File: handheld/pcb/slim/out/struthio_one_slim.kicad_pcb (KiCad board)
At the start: 2 copper layers, 67.6 x 105.2 mm, 12 parts, among them J1 Header_2x16_Waveshare, J2 S2B-PH-K-S, Q1 AO3401A, Q2 AO3400A, SW1 TS-1187A-B-A-B, SW2 TS-1187A-B-A-B, SW3 TS-1187A-B-A-B, SW4 TS-1187A-B-A-B, SW5 SS-12D06-G030

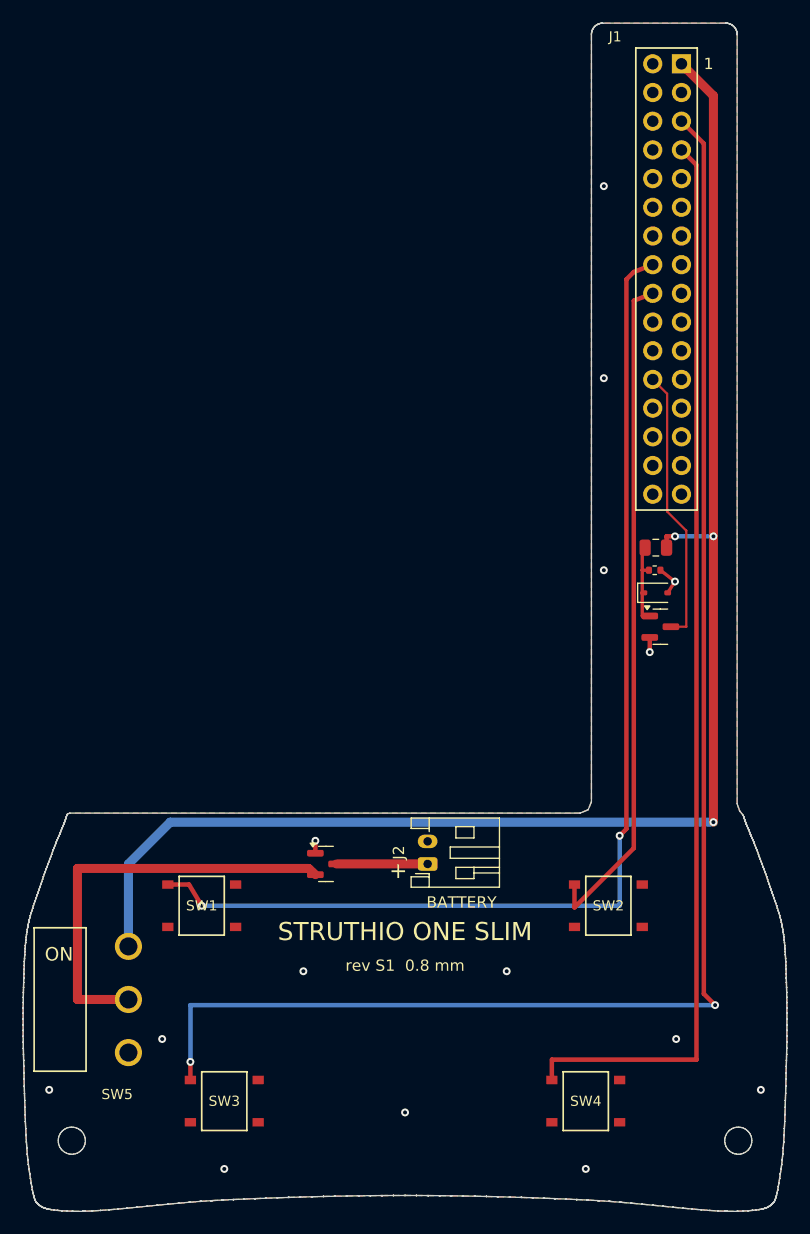
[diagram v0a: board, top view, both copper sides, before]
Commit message: ONE SLIM rev S2 hardware (foolproof) and ONE board rev D
SLIM case: no slide switch; a printed plunger in the left wall presses the Waveshare's
PWR key; one screw size (5 x M2 x 6 countersunk); surface-mount battery socket (no
leads to trim); lead clips; pins stand 3.6 mm out so either socket height works
(3.6 / 2.5 mm into J8), no spacer, no measuring; keyed pin jig (fence + two pegs a
turned-over board cannot sit on) with an 11 mm axle gauge; panel jig. 61 checks pass.
SLIM board rev S2: SW1-4, J2 (C295747), Q1 only, all surface-mount; pin 9 open.
ONE board rev D: header pin 9 tied to GND (the firmware's model strap).
Both boards: DRC no errors, no unconnected pads.

Co-Authored-By: Claude Opus 5.5 <noreply@anthropic.com>
Claude-Session: https://claude.ai/code/session_01BN2x2AjDXTm5ZbuwkUnxX5
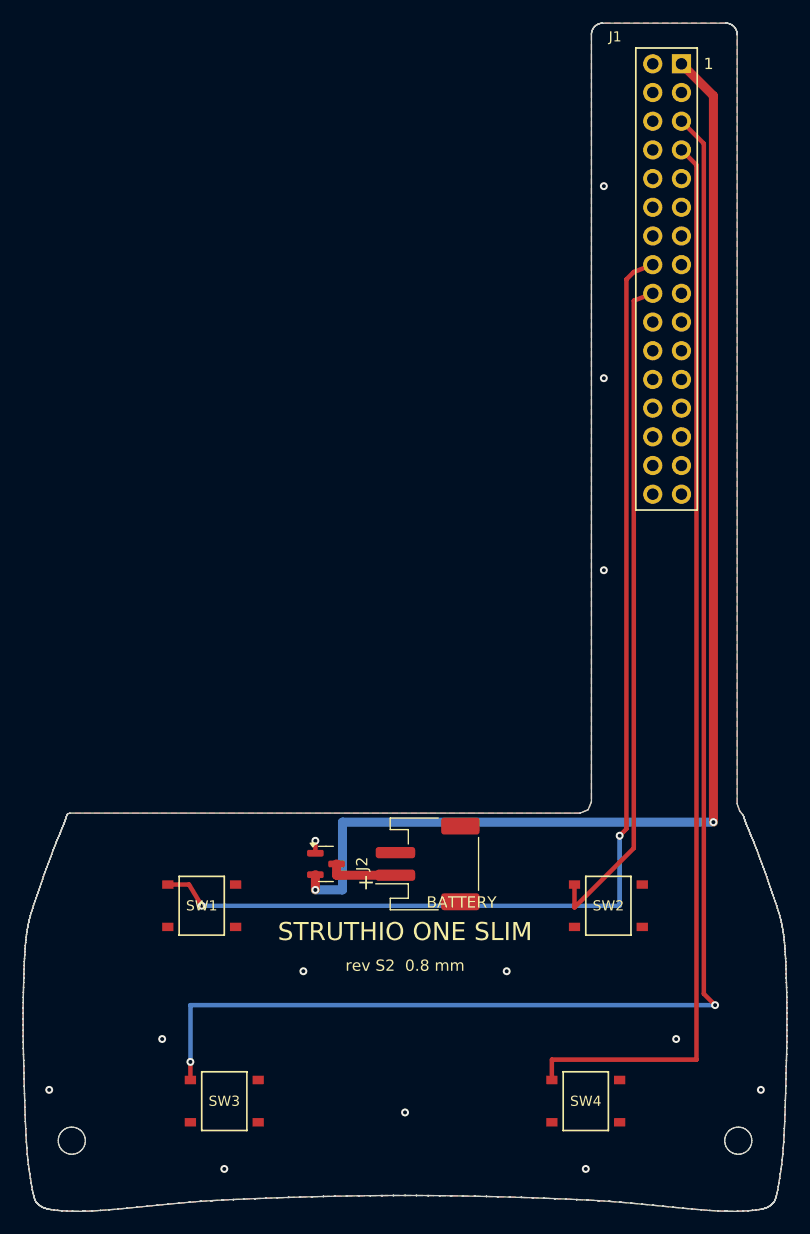
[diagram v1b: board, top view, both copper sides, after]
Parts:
- removed C1: 10uF, C_0805_2012Metric
- removed D1: 1N4148WS, D_SOD-323
- removed Q2: AO3400A, SOT-23
- removed R1: 470k, R_0402_1005Metric
- removed SW5: SS-12D06-G030, STRUTHIO:SS-12D06-G030
- J2: value S2B-PH-K-S -> S2B-PH-SM4-TB; footprint JST_PH_S2B-PH-K_1x02_P2.00mm_Horizontal -> JST_PH_S2B-PH-SM4-TB_1x02-1MP_P2.00mm_Horizontal
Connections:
- J1 pad 24: PWRON -> (no net)
- Q1 pad 2: BAT_RAW -> BAT
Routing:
- net BAT_RAW: track 37.4 -> 0.00 mm
- net PWRON: track 24.5 -> 0.00 mm
- net BAT: track 134.1 -> 110.9 mm, vias 3 -> 2
- net PG: track 7.70 -> 0.00 mm
- net GND: track 5.22 -> 1.10 mm, vias 15 -> 13
- net BAT_IN: track 8.06 -> 6.21 mm
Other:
- board text added: "J1: PINS 1-7 ODD + 4-18 EVEN, 9 EMPTY"
- board text added: "USE THE PRINTED PIN JIG"
- board text added: "rev S2 0.8 mm"
- board text removed: "J1: PINS 1 3 4 5 7 16 18 24 ONLY"
- board text removed: "ON"
- board text removed: "PINS 3.0 MM OUT OF THE FRONT"
- board text removed: "rev S1 0.8 mm"

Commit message: ONE SLIM rev S4: no soldering
The two solder jobs are gone. JLCPCB now fits the header with the other parts: two
surface-mount 2x5 headers (Ckmtw B-2100N10P-B110, C124391) on pins 1-10 and 15-24, a free
row between them. The speaker is a plug-in 1 W cavity speaker with its own 1.25 mm plug.

The header plastic and the socket's 5 mm depth set the stack: the pins go 3.6 mm into J8
(2.5 mm into an 11.5 mm socket), the plastic stands 2.4 mm off the socket. The case is
22.2 mm (limit 23). The extra depth takes the ONE's 1000 mAh THOR-503450 on the back wall,
so the firmware charges the SLIM at 200 mA too. All five screws are M2 x 12. The back
edge round is 3 x 7.5 mm. The pin jig is gone (a small axle gauge is left), and so are three
stale jig STLs that the 3D package was still picking up.

Board rev S4: DRC 0 errors, 0 unconnected; 8 parts, all surface-mount, all assembled.
CAD: 67 checks pass. Firmware builds; host test passes.

Co-Authored-By: Claude Opus 5.5 <noreply@anthropic.com>
Claude-Session: https://claude.ai/code/session_01BN2x2AjDXTm5ZbuwkUnxX5
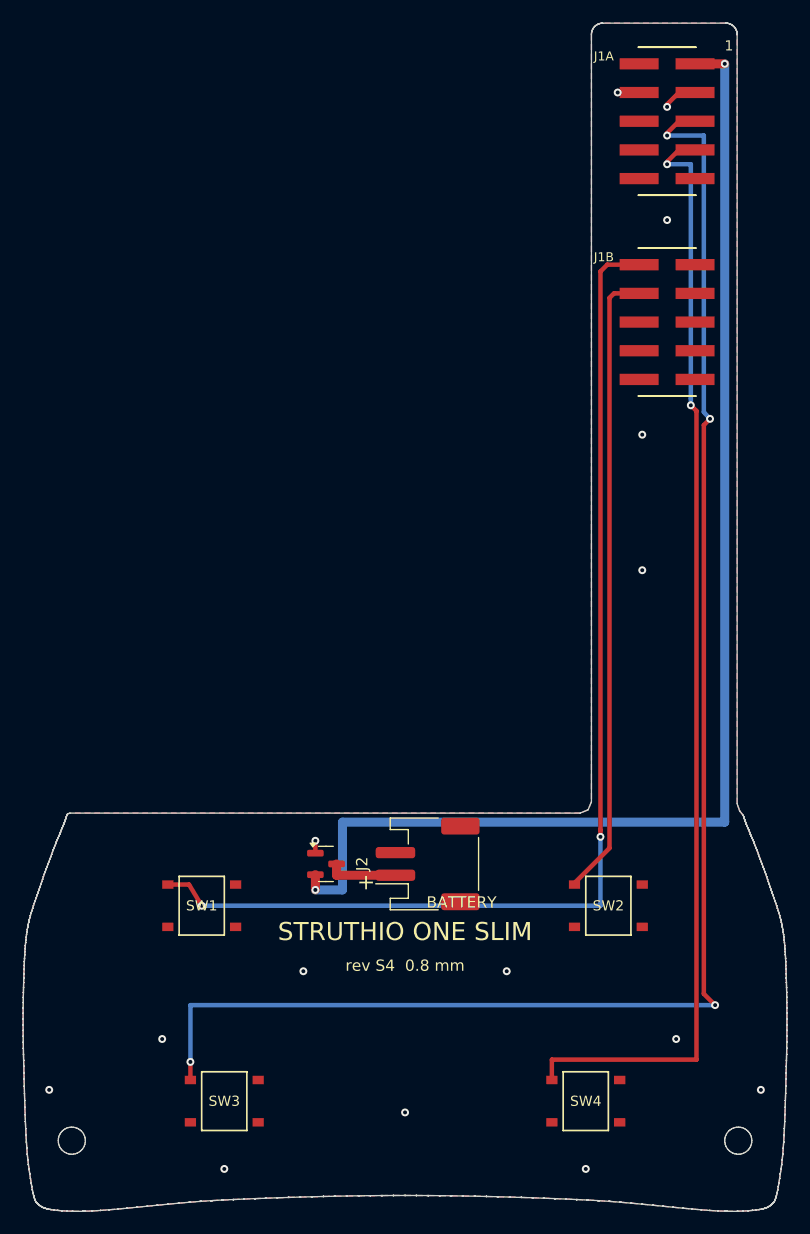
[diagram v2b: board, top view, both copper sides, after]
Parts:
- removed J1: Header_2x16_Waveshare, STRUTHIO:Header_2x16_Waveshare
- added J1A: B-2100N10P-B110, STRUTHIO:PinHeader_2x05_P2.54mm_SMD_Ckmtw210SMT, F.Cu at (123.2, 72.2)
- added J1B: B-2100N10P-B110, STRUTHIO:PinHeader_2x05_P2.54mm_SMD_Ckmtw210SMT, F.Cu at (123.2, 90.0)
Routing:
- net GPIO18: track 59.7 -> 54.6 mm
- net GND: track 1.10 -> 4.70 mm, vias 13 -> 15
- net GPIO21: track 132.6 -> 135.9 mm, vias 2 -> 4
- net BAT: track 110.9 -> 113.3 mm
- net GPIO38: track 95.7 -> 97.9 mm, vias 0 -> 2
- net GPIO17: track 99.5 -> 97.8 mm
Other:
- board text added: "EVERY PART FITTED BY JLCPCB"
- board text added: "NO SOLDERING"
- board text added: "rev S4 0.8 mm"
- board text removed: "J1: PINS 1-7 ODD + 4-18 EVEN, 9 EMPTY"
- board text removed: "USE THE PRINTED PIN JIG"
- board text removed: "rev S2 0.8 mm"

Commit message: Back to the 16.5 mm ONE SLIM (rev S3), with a plug-in speaker
Reverts rev S4 (22.2 mm, no soldering): the goal is the 16.5 mm rounded-edge
SLIM, as easy as possible.

At 16.5 mm the speaker no longer needs soldering. A 1 W 8 ohm mini cavity
speaker with its own 1.25 mm plug (about 15 x 10 x 3.6 mm) sits on the back
wall, 0.3 mm clear of the Waveshare's parts, and plugs straight into J9. The
12 header pins are the only soldering left. CAD: 68 checks pass.

Kept from S4: the three stale jig STLs removed from cad/slim/stl (the 3D
package was shipping them), the ONE manual's broken quote fixed (it had not
built since S3), and tools/visuals/side_by_side.py, which labels the side by
side picture from the models' real depths. Manuals, quick-start card, step
pictures and animation rebuilt.

Co-Authored-By: Claude Opus 5.5 <noreply@anthropic.com>
Claude-Session: https://claude.ai/code/session_01BN2x2AjDXTm5ZbuwkUnxX5
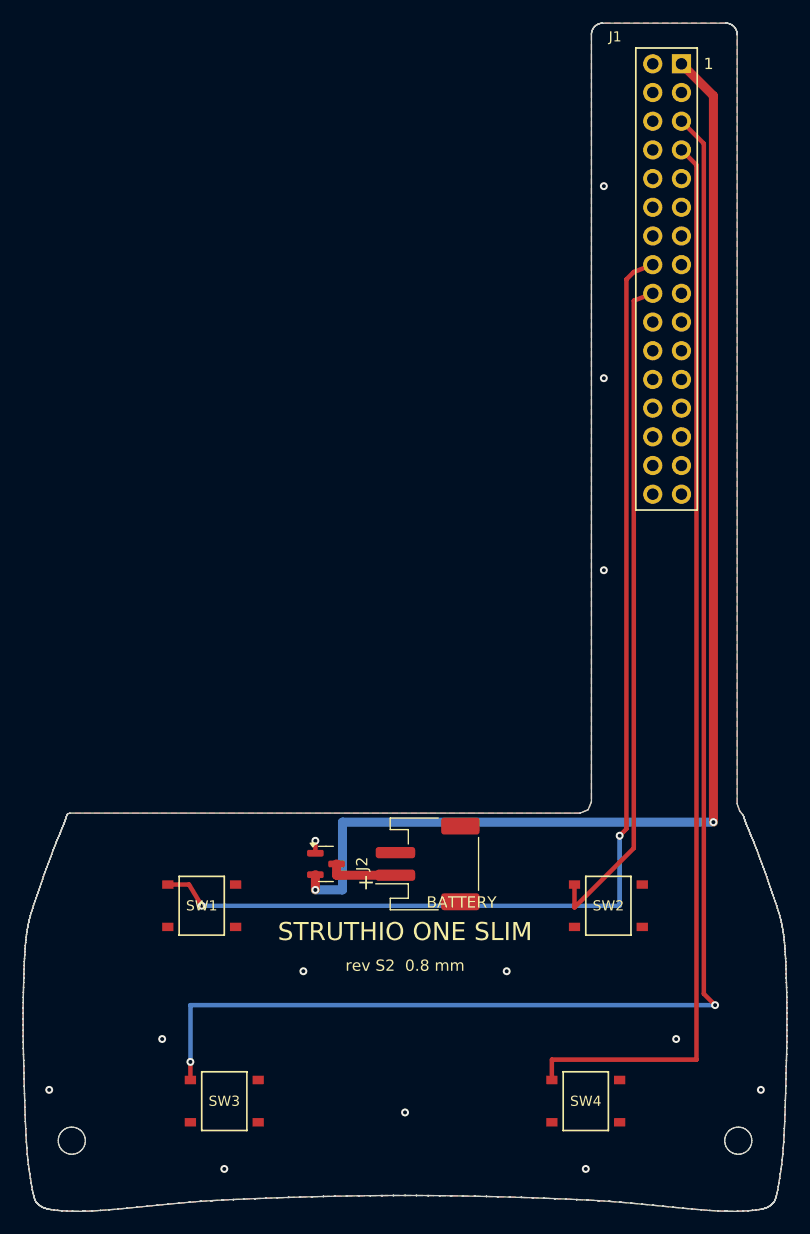
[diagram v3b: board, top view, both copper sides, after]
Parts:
- removed J1A, J1B: B-2100N10P-B110, STRUTHIO:PinHeader_2x05_P2.54mm_SMD_Ckmtw210SMT
- added J1: Header_2x16_Waveshare, STRUTHIO:Header_2x16_Waveshare, F.Cu at (123.2, 86.2)
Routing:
- net GPIO18: track 54.6 -> 59.7 mm
- net GND: track 4.70 -> 1.10 mm, vias 15 -> 13
- net GPIO21: track 135.9 -> 132.6 mm, vias 4 -> 2
- net BAT: track 113.3 -> 110.9 mm
- net GPIO38: track 97.9 -> 95.7 mm, vias 2 -> 0
- net GPIO17: track 97.8 -> 99.5 mm
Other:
- board text added: "J1: PINS 1-7 ODD + 4-18 EVEN, 9 EMPTY"
- board text added: "USE THE PRINTED PIN JIG"
- board text added: "rev S2 0.8 mm"
- board text removed: "EVERY PART FITTED BY JLCPCB"
- board text removed: "NO SOLDERING"
- board text removed: "rev S4 0.8 mm"
